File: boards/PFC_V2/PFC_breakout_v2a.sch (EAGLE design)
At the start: 33 parts, among them CN1 1X4-BIG

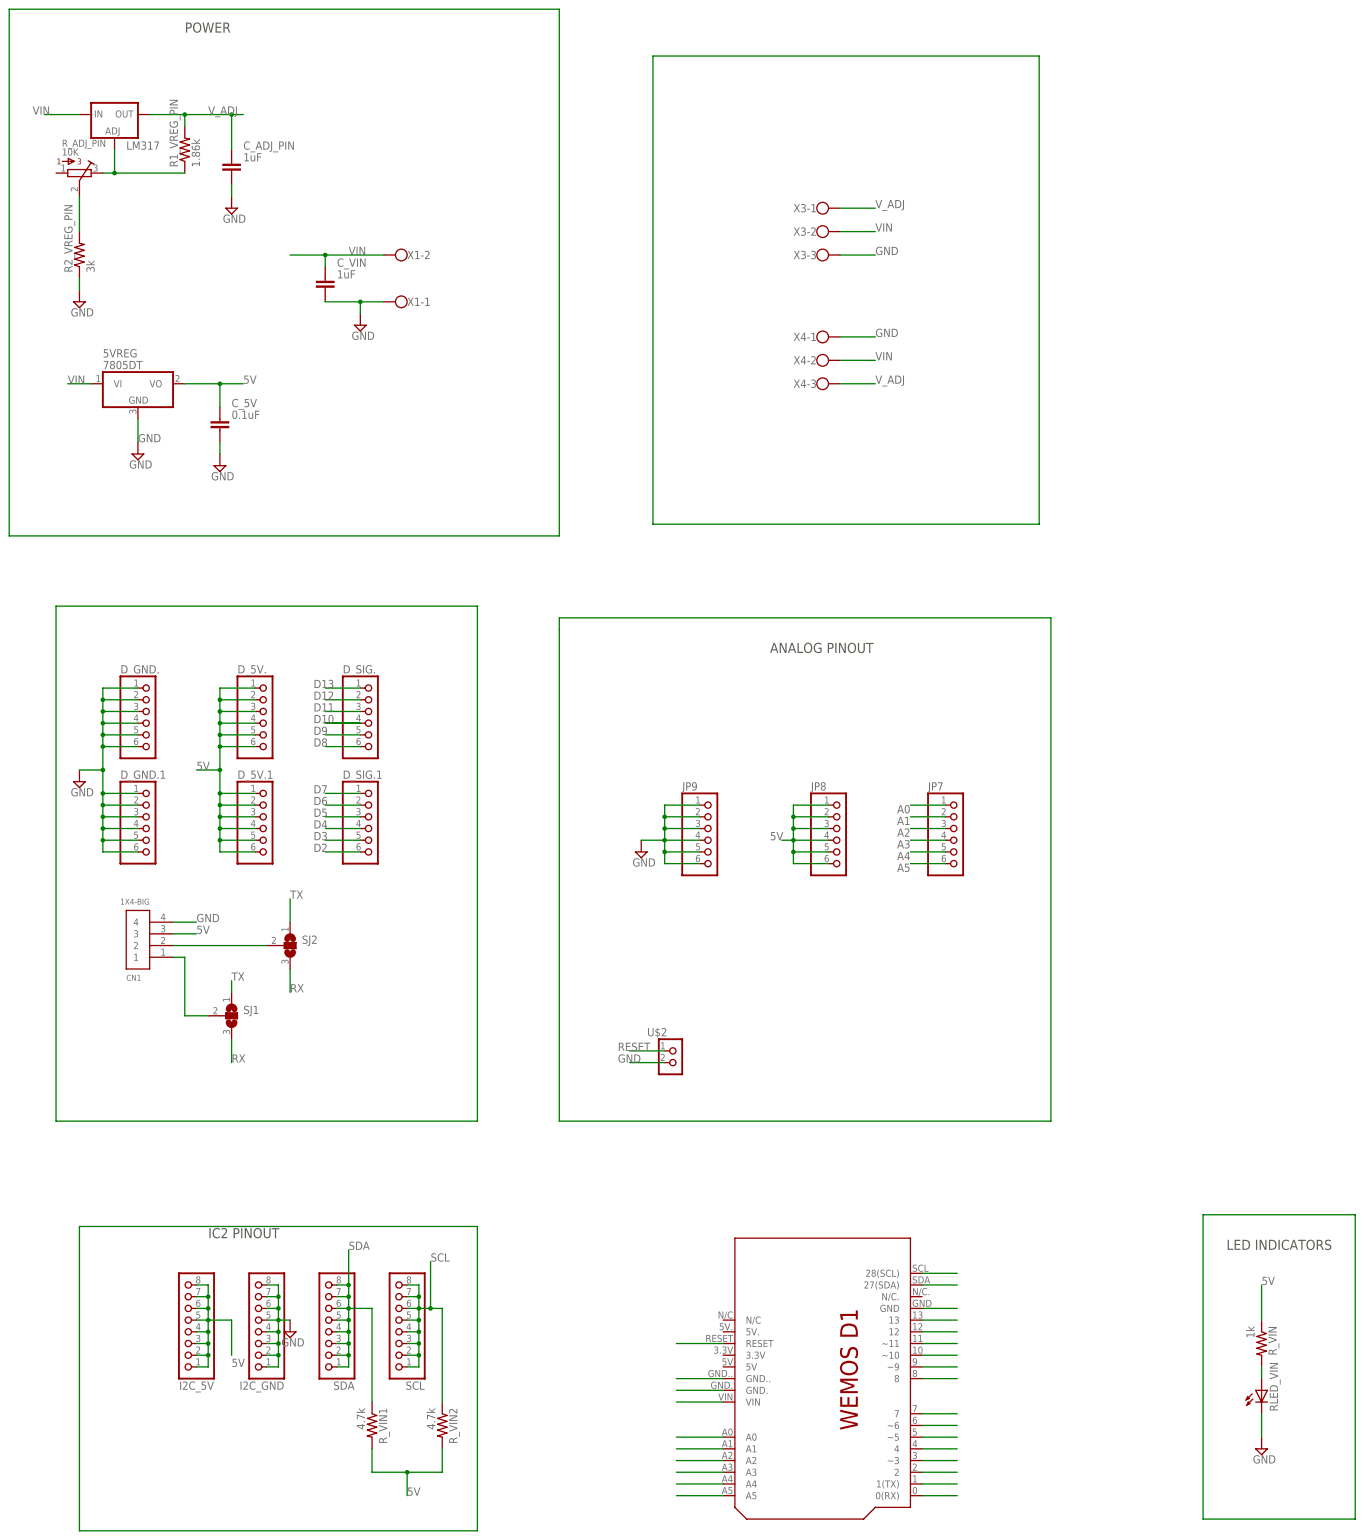
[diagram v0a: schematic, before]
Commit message: completed ui of touch screen. No integration yet
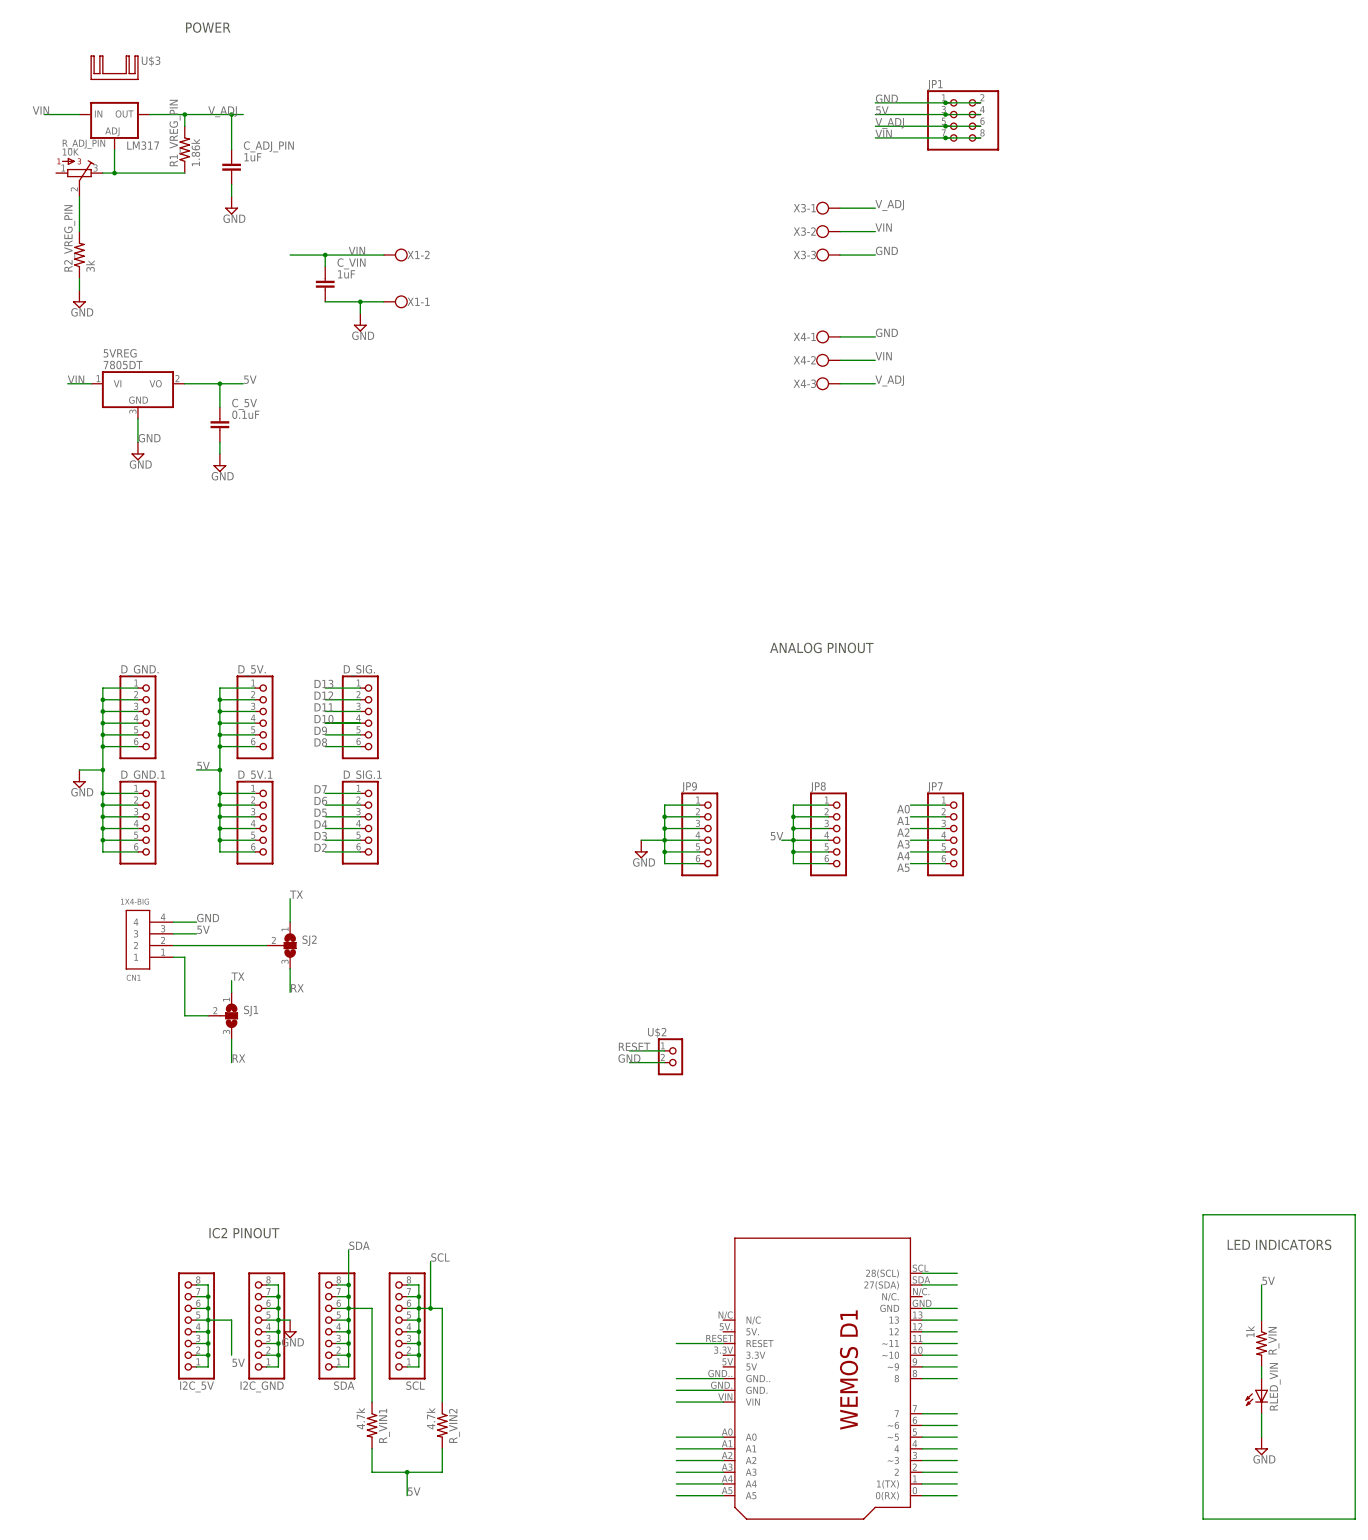
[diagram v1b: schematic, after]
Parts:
- added JP1: (no value), adafruit:PINHD-2X4
- added U$3: FW1S, heatsink:FW1S
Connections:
- net 5V: now also JP1.3, JP1.4
- net GND: now also JP1.1, JP1.2
- net VIN: now also JP1.7, JP1.8
- net V_ADJ: now also JP1.5, JP1.6
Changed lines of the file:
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@@
 <layer number="110" name="fp0" color="7" fill="1" visible="no" active="yes"/>
 <layer number="111" name="LPC17xx" color="7" fill="1" visible="no" active="yes"/>
-<layer number="112" name="tSilk" color="7" fill="1" visible="no" active="yes"/>
+<layer number="112" name="tSilk" color="7" fill="1" visible="yes" active="yes"/>
 <layer number="113" name="ReferenceLS" color="7" fill="1" visible="no" active="no"/>
 <layer number="114" name="Badge_Outline" color="11" fill="1" visible="no" active="no"/>
@@
 <part name="D_5V.1" library="adafruit" deviceset="PINHD-1X6" device=""/>
 <part name="D_SIG.1" library="adafruit" deviceset="PINHD-1X6" device=""/>
+<part name="U$3" library="heatsink" deviceset="FW1S" device=""/>
+<part name="JP1" library="adafruit" deviceset="PINHD-2X4" device=""/>
 </parts>
 <sheets>
@@
 <text x="-213.36" y="66.04" size="2.1844" layer="97">POWER</text>
 <text x="12.7" y="-198.12" size="2.1844" layer="97">LED INDICATORS</text>
+<wire x1="-104.14" y1="63.5" x2="-104.14" y2="-33.02" width="0.1524" layer="112"/>
+<wire x1="-104.14" y1="-33.02" x2="-10.16" y2="-33.02" width="0.1524" layer="112"/>
+<wire x1="-10.16" y1="-33.02" x2="-10.16" y2="63.5" width="0.1524" layer="112"/>
+<wire x1="-10.16" y1="63.5" x2="-104.14" y2="63.5" width="0.1524" layer="112"/>
+<wire x1="-256.54" y1="-45.72" x2="-144.78" y2="-45.72" width="0.1524" layer="112"/>
+<wire x1="-144.78" y1="-45.72" x2="-144.78" y2="76.2" width="0.1524" layer="112"/>
+<wire x1="-144.78" y1="76.2" x2="-256.54" y2="76.2" width="0.1524" layer="112"/>
+<wire x1="-256.54" y1="76.2" x2="-256.54" y2="-45.72" width="0.1524" layer="112"/>
+<wire x1="-134.62" y1="-58.42" x2="-134.62" y2="-167.64" width="0.1524" layer="112"/>
+<wire x1="-134.62" y1="-167.64" x2="-30.48" y2="-167.64" width="0.1524" layer="112"/>
+<wire x1="-30.48" y1="-167.64" x2="-30.48" y2="-58.42" width="0.1524" layer="112"/>
+<wire x1="-30.48" y1="-58.42" x2="-134.62" y2="-58.42" width="0.1524" layer="112"/>
+<wire x1="-251.46" y1="-55.88" x2="-152.4" y2="-55.88" width="0.1524" layer="112"/>
+<wire x1="-152.4" y1="-55.88" x2="-152.4" y2="-165.1" width="0.1524" layer="112"/>
+<wire x1="-152.4" y1="-165.1" x2="-251.46" y2="-165.1" width="0.1524" layer="112"/>
+<wire x1="-251.46" y1="-165.1" x2="-251.46" y2="-55.88" width="0.1524" layer="112"/>
+<wire x1="-220.98" y1="-185.42" x2="-137.16" y2="-185.42" width="0.1524" layer="112"/>
+<wire x1="-137.16" y1="-185.42" x2="-137.16" y2="-261.62" width="0.1524" layer="112"/>
+<wire x1="-137.16" y1="-261.62" x2="-220.98" y2="-261.62" width="0.1524" layer="112"/>
+<wire x1="-220.98" y1="-261.62" x2="-220.98" y2="-185.42" width="0.1524" layer="112"/>
 </plain>
 <instances>
@@
 <instance part="D_5V.1" gate="A" x="-195.58" y="-106.68"/>
 <instance part="D_SIG.1" gate="A" x="-172.72" y="-106.68"/>
+<instance part="U$3" gate="G$1" x="-228.6" y="55.88"/>
+<instance part="JP1" gate="A" x="-45.72" y="45.72"/>
 </instances>
 <busses>
@@
 <label x="-63.5" y="17.78" size="1.778" layer="95"/>
 </segment>
-</net>
-<net name="ADJ_SWITCH" class="0">
-<segment>
-<wire x1="-251.46" y1="71.12" x2="-132.08" y2="71.12" width="0.1524" layer="91"/>
-<wire x1="-132.08" y1="71.12" x2="-132.08" y2="-43.18" width="0.1524" layer="91"/>
-<wire x1="-251.46" y1="71.12" x2="-251.46" y2="-43.18" width="0.1524" layer="91"/>
-<wire x1="-251.46" y1="-43.18" x2="-132.08" y2="-43.18" width="0.1524" layer="91"/>
+<segment>
+<pinref part="JP1" gate="A" pin="2"/>
+<pinref part="JP1" gate="A" pin="1"/>
+<wire x1="-40.64" y1="50.8" x2="-48.26" y2="50.8" width="0.1524" layer="91"/>
+<wire x1="-48.26" y1="50.8" x2="-63.5" y2="50.8" width="0.1524" layer="91"/>
+<junction x="-48.26" y="50.8"/>
+<label x="-63.5" y="50.8" size="1.778" layer="95"/>
 </segment>
 </net>
@@
 <pinref part="U$1" gate="G$1" pin="VIN"/>
 <wire x1="-96.52" y1="-231.14" x2="-106.68" y2="-231.14" width="0.1524" layer="91"/>
+</segment>
+<segment>
+<pinref part="JP1" gate="A" pin="8"/>
+<pinref part="JP1" gate="A" pin="7"/>
+<wire x1="-40.64" y1="43.18" x2="-48.26" y2="43.18" width="0.1524" layer="91"/>
+<wire x1="-48.26" y1="43.18" x2="-63.5" y2="43.18" width="0.1524" layer="91"/>
+<junction x="-48.26" y="43.18"/>
+<label x="-63.5" y="43.18" size="1.778" layer="95"/>
 </segment>
 </net>
@@
 <label x="20.32" y="-205.74" size="1.778" layer="95"/>
 </segment>
+<segment>
+<pinref part="JP1" gate="A" pin="3"/>
+<pinref part="JP1" gate="A" pin="4"/>
+<wire x1="-48.26" y1="48.26" x2="-40.64" y2="48.26" width="0.1524" layer="91"/>
+<wire x1="-48.26" y1="48.26" x2="-63.5" y2="48.26" width="0.1524" layer="91"/>
+<junction x="-48.26" y="48.26"/>
+<label x="-63.5" y="48.26" size="1.778" layer="95"/>
+</segment>
 </net>
 <net name="A5" class="0">
@@
 <pinref part="R_VIN" gate="G$1" pin="2"/>
 <wire x1="20.32" y1="-226.06" x2="20.32" y2="-223.52" width="0.1524" layer="91"/>
-</segment>
-</net>
-<net name="N$10" class="0">
-<segment>
-<wire x1="-236.22" y1="-193.04" x2="-149.86" y2="-193.04" width="0.1524" layer="91"/>
-<wire x1="-149.86" y1="-193.04" x2="-149.86" y2="-259.08" width="0.1524" layer="91"/>
-<wire x1="-149.86" y1="-259.08" x2="-236.22" y2="-259.08" width="0.1524" layer="91"/>
-<wire x1="-236.22" y1="-259.08" x2="-236.22" y2="-193.04" width="0.1524" layer="91"/>
 </segment>
 </net>
@@
 <wire x1="-71.12" y1="27.94" x2="-63.5" y2="27.94" width="0.1524" layer="91"/>
 <label x="-63.5" y="27.94" size="1.778" layer="95"/>
+</segment>
+<segment>
+<pinref part="JP1" gate="A" pin="6"/>
+<pinref part="JP1" gate="A" pin="5"/>
+<wire x1="-40.64" y1="45.72" x2="-48.26" y2="45.72" width="0.1524" layer="91"/>
+<wire x1="-48.26" y1="45.72" x2="-63.5" y2="45.72" width="0.1524" layer="91"/>
+<junction x="-48.26" y="45.72"/>
+<label x="-63.5" y="45.72" size="1.778" layer="95"/>
 </segment>
 </net>
@@
 </segment>
 </net>
-<net name="N$4" class="0">
-<segment>
-<wire x1="-241.3" y1="-58.42" x2="-149.86" y2="-58.42" width="0.1524" layer="91"/>
-<wire x1="-149.86" y1="-58.42" x2="-149.86" y2="-170.18" width="0.1524" layer="91"/>
-<wire x1="-149.86" y1="-170.18" x2="-241.3" y2="-170.18" width="0.1524" layer="91"/>
-<wire x1="-241.3" y1="-170.18" x2="-241.3" y2="-58.42" width="0.1524" layer="91"/>
-</segment>
-</net>
-<net name="N$5" class="0">
-<segment>
-<wire x1="-132.08" y1="-63.5" x2="-132.08" y2="-170.18" width="0.1524" layer="91"/>
-<wire x1="-132.08" y1="-170.18" x2="-25.4" y2="-170.18" width="0.1524" layer="91"/>
-<wire x1="-25.4" y1="-170.18" x2="-25.4" y2="-60.96" width="0.1524" layer="91"/>
-<wire x1="-25.4" y1="-60.96" x2="-132.08" y2="-60.96" width="0.1524" layer="91"/>
-<wire x1="-132.08" y1="-60.96" x2="-132.08" y2="-63.5" width="0.1524" layer="91"/>
-</segment>
-</net>
-<net name="N$6" class="0">
-<segment>
-<wire x1="-111.76" y1="60.96" x2="-111.76" y2="-40.64" width="0.1524" layer="91"/>
-<wire x1="-111.76" y1="-40.64" x2="-27.94" y2="-40.64" width="0.1524" layer="91"/>
-<wire x1="-27.94" y1="-40.64" x2="-27.94" y2="60.96" width="0.1524" layer="91"/>
-<wire x1="-27.94" y1="60.96" x2="-111.76" y2="60.96" width="0.1524" layer="91"/>
-</segment>
-</net>

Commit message: boards and src
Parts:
- removed 5VREG: 7805DT, adafruit:7805DT
- removed C_5V: 0.1uF, dp_devices:CAPACITOR_NPOL-0603
- removed C_ADJ_PIN, C_VIN: 1uF, dp_devices:CAPACITOR_NPOL-0603
- removed LM317: (no value), v-reg:LM317TS
- removed R1_VREG_PIN: 1.86k, resistor:R-US_R0603
- removed R2_VREG_PIN: 3k, resistor:R-US_R0603
- removed R_ADJ_PIN: 10K, bourns:3386-P
- removed X1: (no value), con-wago-500:W237-102
- removed X3, X4: (no value), con-wago-500:W237-103
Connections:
- removed net N$23: LM317.ADJ, R1_VREG_PIN.1, R_ADJ_PIN.3
- removed net N$24: R2_VREG_PIN.2, R_ADJ_PIN.2
- net 5V: no longer 5VREG.VO, C_5V.1
- net GND: no longer 5VREG.GND, C_5V.2, C_ADJ_PIN.2, C_VIN.2, R2_VREG_PIN.1, X1-1.KL, X3-3.KL, X4-1.KL
- net VIN: no longer 5VREG.VI, C_VIN.1, LM317.IN, X1-2.KL, X3-2.KL, X4-2.KL
- net V_ADJ: no longer C_ADJ_PIN.1, LM317.OUT, R1_VREG_PIN.2, X3-1.KL, X4-3.KL
